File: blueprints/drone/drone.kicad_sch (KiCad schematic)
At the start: 9 parts, among them J1 Connector battery, J2 Motor 1 IN, J3 ESC 1 OUT, J4 ESC 2 OUT, J5 Motor 2 IN, J6 ESC 3 OUT, J7 ESC 0 OUT, J8 Motor 3 IN, J9 Motor 0 IN

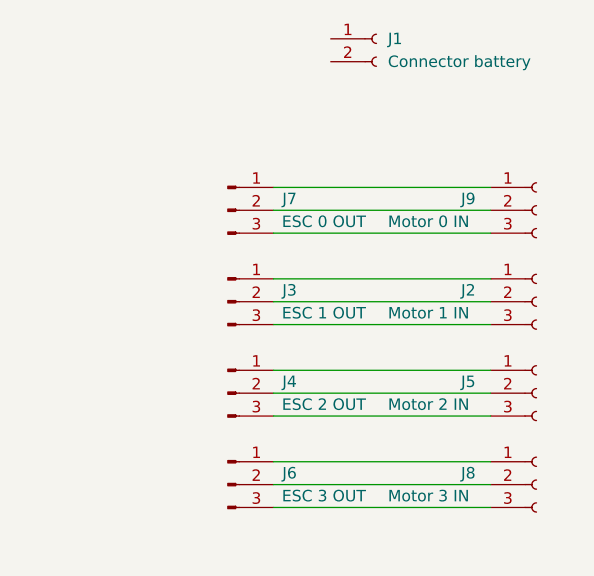
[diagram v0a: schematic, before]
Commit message: Added power distribution from battery to esc
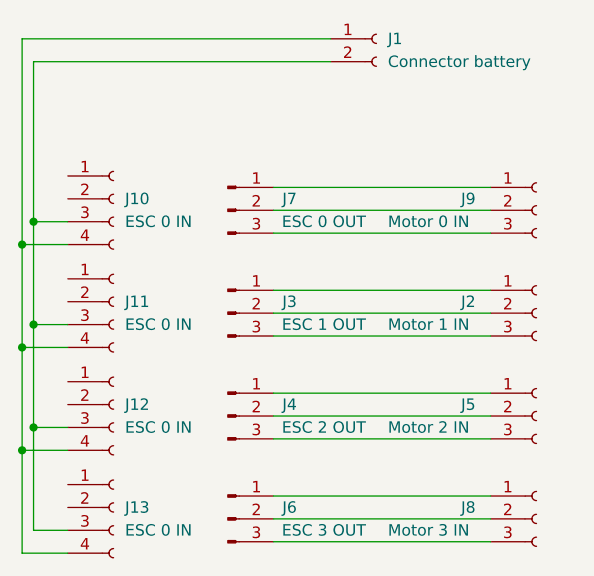
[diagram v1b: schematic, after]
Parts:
- added J10, J11, J12, J13: ESC 0 IN, Connector_PinHeader_1.27mm:PinHeader_1x04_P1.27mm_Vertical, symbol Connector:Conn_01x04_Socket
- J1: footprint (none) -> Connector_JST:JST_XH_B2B-XH-A_1x02_P2.50mm_Vertical
- J2, J5, J8, J9: footprint (none) -> Connector_JST:JST_XH_B3B-XH-A_1x03_P2.50mm_Vertical
- J3, J4, J6, J7: footprint (none) -> Connector_PinHeader_2.00mm:PinHeader_1x03_P2.00mm_Vertical
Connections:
- net at J1.1 (Pin_1): now also J10.4 (Pin_4), J11.4 (Pin_4), J12.4 (Pin_4), J13.4 (Pin_4)
- net at J1.2 (Pin_2): now also J10.3 (Pin_3), J11.3 (Pin_3), J12.3 (Pin_3), J13.3 (Pin_3)
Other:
- moved on the sheet: J2, J3, J4, J5, J6, J8

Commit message: Updated pcb design
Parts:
- removed J3: ESC 1 OUT, Connector_PinHeader_2.00mm:PinHeader_1x03_P2.00mm_Vertical, symbol Connector:Conn_01x03_Pin
- removed J4: ESC 2 OUT, Connector_PinHeader_2.00mm:PinHeader_1x03_P2.00mm_Vertical, symbol Connector:Conn_01x03_Pin
- removed J6: ESC 3 OUT, Connector_PinHeader_2.00mm:PinHeader_1x03_P2.00mm_Vertical, symbol Connector:Conn_01x03_Pin
- removed J7: ESC 0 OUT, Connector_PinHeader_2.00mm:PinHeader_1x03_P2.00mm_Vertical, symbol Connector:Conn_01x03_Pin
- added J14, J3, J4, J7: ESC 0 OUT, Connector_PinHeader_2.00mm:PinHeader_1x03_P2.00mm_Vertical, symbol Connector:Conn_01x03_Socket
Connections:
- net at J5.1 (Pin_1): now also J3.3 (Pin_3)
- net at J5.2 (Pin_2): now also J3.2 (Pin_2)
- net at J5.3 (Pin_3): now also J3.1 (Pin_1)
- net at J9.1 (Pin_1): now also J14.3 (Pin_3)
- net at J9.2 (Pin_2): now also J14.2 (Pin_2)
- net at J9.3 (Pin_3): now also J14.1 (Pin_1)
- net at J2.1 (Pin_1): now also J7.3 (Pin_3)
- net at J2.2 (Pin_2): now also J7.2 (Pin_2)
- net at J2.3 (Pin_3): now also J7.1 (Pin_1)
- net at J8.1 (Pin_1): now also J4.3 (Pin_3)
- net at J8.2 (Pin_2): now also J4.2 (Pin_2)
- net at J8.3 (Pin_3): now also J4.1 (Pin_1)
